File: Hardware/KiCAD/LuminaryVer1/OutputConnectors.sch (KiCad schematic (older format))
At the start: 2 parts, among them J13 CN1, J14 CN2

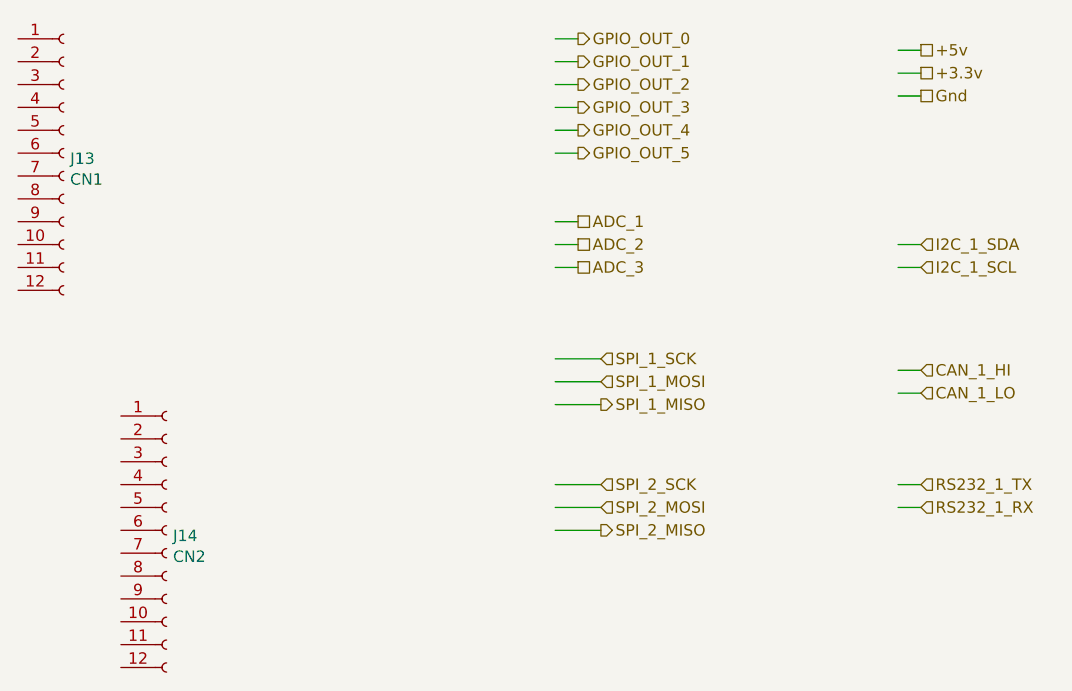
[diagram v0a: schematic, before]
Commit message: Added majority of the logic level circuitry. Almost done routing connections.
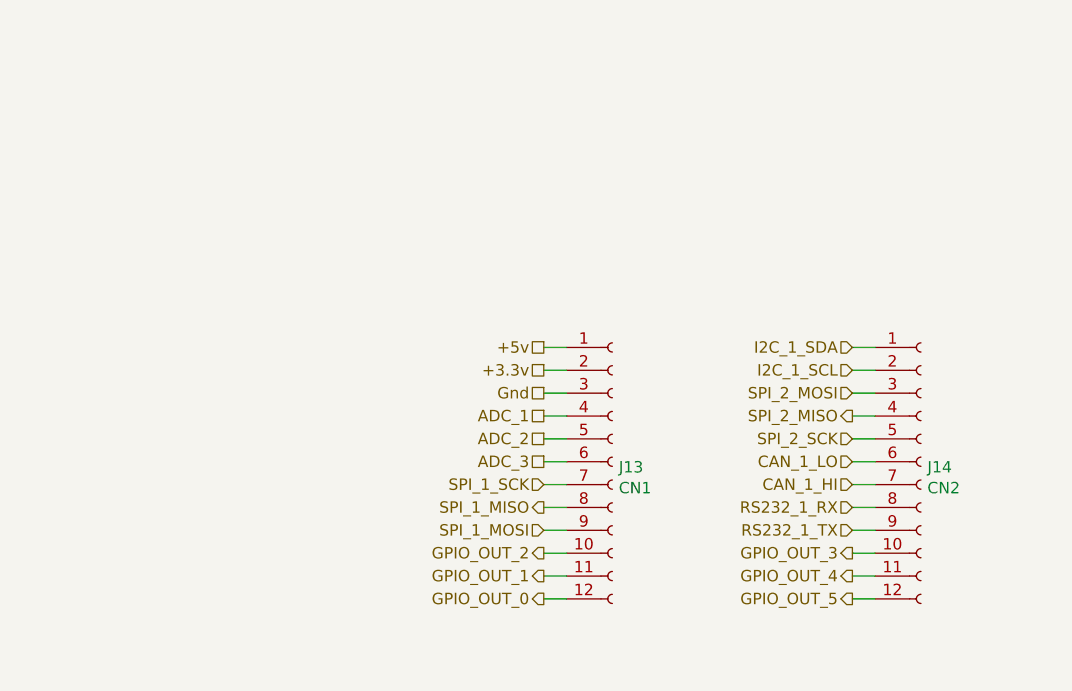
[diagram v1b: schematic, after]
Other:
- moved on the sheet: J13, J14
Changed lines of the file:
@@
 Comment4 ""
 $EndDescr
-Text HLabel 5100 3400 2    50   Input ~ 0
+Text HLabel 4850 3950 0    50   Input ~ 0
 SPI_1_SCK
-Text HLabel 5100 3500 2    50   Input ~ 0
+Text HLabel 4850 4150 0    50   Input ~ 0
 SPI_1_MOSI
-Text HLabel 5100 3600 2    50   Output ~ 0
+Text HLabel 4850 4050 0    50   Output ~ 0
 SPI_1_MISO
-Text HLabel 5100 3950 2    50   Input ~ 0
+Text HLabel 6200 3750 0    50   Input ~ 0
 SPI_2_SCK
-Text HLabel 5100 4050 2    50   Input ~ 0
+Text HLabel 6200 3550 0    50   Input ~ 0
 SPI_2_MOSI
-Text HLabel 5100 4150 2    50   Output ~ 0
+Text HLabel 6200 3650 0    50   Output ~ 0
 SPI_2_MISO
-Text HLabel 6500 2900 2    50   Input ~ 0
+Text HLabel 6200 3350 0    50   Input ~ 0
 I2C_1_SDA
-Text HLabel 6500 3000 2    50   Input ~ 0
+Text HLabel 6200 3450 0    50   Input ~ 0
 I2C_1_SCL
-Text HLabel 6500 3950 2    50   Input ~ 0
+Text HLabel 6200 4150 0    50   Input ~ 0
 RS232_1_TX
-Text HLabel 6500 4050 2    50   Input ~ 0
+Text HLabel 6200 4050 0    50   Input ~ 0
 RS232_1_RX
-Text HLabel 6500 3450 2    50   Input ~ 0
+Text HLabel 6200 3950 0    50   Input ~ 0
 CAN_1_HI
-Text HLabel 6500 3550 2    50   Input ~ 0
+Text HLabel 6200 3850 0    50   Input ~ 0
 CAN_1_LO
-Text HLabel 5000 2800 2    50   UnSpc ~ 0
+Text HLabel 4850 3650 0    50   UnSpc ~ 0
 ADC_1
-Text HLabel 5000 2900 2    50   UnSpc ~ 0
+Text HLabel 4850 3750 0    50   UnSpc ~ 0
 ADC_2
-Text HLabel 5000 3000 2    50   UnSpc ~ 0
+Text HLabel 4850 3850 0    50   UnSpc ~ 0
 ADC_3
-Wire Wire Line
-	4900 3400 5100 3400
-Wire Wire Line
-	4900 3500 5100 3500
-Wire Wire Line
-	4900 3600 5100 3600
-Wire Wire Line
-	4900 3950 5100 3950
-Wire Wire Line
-	4900 4050 5100 4050
-Wire Wire Line
-	4900 4150 5100 4150
-Wire Wire Line
-	6400 3450 6500 3450
-Wire Wire Line
-	6400 3550 6500 3550
-Wire Wire Line
-	4900 2800 5000 2800
-Wire Wire Line
-	4900 2900 5000 2900
-Wire Wire Line
-	4900 3000 5000 3000
-Wire Wire Line
-	6400 2900 6500 2900
-Wire Wire Line
-	6400 3000 6500 3000
-Wire Wire Line
-	6400 3950 6500 3950
-Wire Wire Line
-	6400 4050 6500 4050
-Text HLabel 5000 2000 2    50   Output ~ 0
+Text HLabel 4850 4450 0    50   Output ~ 0
 GPIO_OUT_0
-Text HLabel 5000 2100 2    50   Output ~ 0
+Text HLabel 4850 4350 0    50   Output ~ 0
 GPIO_OUT_1
-Text HLabel 5000 2200 2    50   Output ~ 0
+Text HLabel 4850 4250 0    50   Output ~ 0
 GPIO_OUT_2
-Text HLabel 5000 2300 2    50   Output ~ 0
+Text HLabel 6200 4250 0    50   Output ~ 0
 GPIO_OUT_3
-Text HLabel 5000 2400 2    50   Output ~ 0
+Text HLabel 6200 4350 0    50   Output ~ 0
 GPIO_OUT_4
-Text HLabel 5000 2500 2    50   Output ~ 0
+Text HLabel 6200 4450 0    50   Output ~ 0
 GPIO_OUT_5
-Wire Wire Line
-	4900 2000 5000 2000
-Wire Wire Line
-	4900 2100 5000 2100
-Wire Wire Line
-	4900 2200 5000 2200
-Wire Wire Line
-	4900 2300 5000 2300
-Wire Wire Line
-	4900 2400 5000 2400
-Wire Wire Line
-	4900 2500 5000 2500
-Text HLabel 6500 2050 2    50   UnSpc ~ 0
+Text HLabel 4850 3350 0    50   UnSpc ~ 0
 +5v
-Text HLabel 6500 2150 2    50   UnSpc ~ 0
+Text HLabel 4850 3450 0    50   UnSpc ~ 0
 +3.3v
-Text HLabel 6500 2250 2    50   UnSpc ~ 0
+Text HLabel 4850 3550 0    50   UnSpc ~ 0
 Gnd
-Wire Wire Line
-	6400 2250 6500 2250
-Wire Wire Line
-	6400 2150 6500 2150
-Wire Wire Line
-	6400 2050 6500 2050
 $Comp
 L Connector:Conn_01x12_Female J13
 U 1 1 5ECB3CF3
-P 2750 2500
-F 0 "J13" H 2778 2476 50  0000 L CNN
-F 1 "CN1" H 2778 2385 50  0000 L CNN
-F 2 "Connector_PinHeader_2.54mm:PinHeader_1x12_P2.54mm_Vertical" H 2750 2500 50  0001 C CNN
-F 3 "~" H 2750 2500 50  0001 C CNN
-	1    2750 2500
+P 5150 3850
+F 0 "J13" H 5178 3826 50  0000 L CNN
+F 1 "CN1" H 5178 3735 50  0000 L CNN
+F 2 "Connector_PinHeader_2.54mm:PinHeader_1x12_P2.54mm_Vertical" H 5150 3850 50  0001 C CNN
+F 3 "~" H 5150 3850 50  0001 C CNN
+	1    5150 3850
 	1    0    0    -1
 $EndComp
@@
 L Connector:Conn_01x12_Female J14
 U 1 1 5ECB51B2
-P 3200 4150
-F 0 "J14" H 3228 4126 50  0000 L CNN
-F 1 "CN2" H 3228 4035 50  0000 L CNN
-F 2 "Connector_PinHeader_2.54mm:PinHeader_1x12_P2.54mm_Vertical" H 3200 4150 50  0001 C CNN
-F 3 "~" H 3200 4150 50  0001 C CNN
-	1    3200 4150
+P 6500 3850
+F 0 "J14" H 6528 3826 50  0000 L CNN
+F 1 "CN2" H 6528 3735 50  0000 L CNN
+F 2 "Connector_PinHeader_2.54mm:PinHeader_1x12_P2.54mm_Vertical" H 6500 3850 50  0001 C CNN
+F 3 "~" H 6500 3850 50  0001 C CNN
+	1    6500 3850
 	1    0    0    -1
 $EndComp
+Wire Wire Line
+	6200 4250 6300 4250
+Wire Wire Line
+	6200 4350 6300 4350
+Wire Wire Line
+	6200 4450 6300 4450
+Wire Wire Line
+	4850 4250 4950 4250
+Wire Wire Line
+	4850 4350 4950 4350
+Wire Wire Line
+	4850 4450 4950 4450
+Wire Wire Line
+	4850 3350 4950 3350
+Wire Wire Line
+	4850 3450 4950 3450
+Wire Wire Line
+	4850 3550 4950 3550
+Wire Wire Line
+	4850 3650 4950 3650
+Wire Wire Line
+	4850 3750 4950 3750
+Wire Wire Line
+	4850 3850 4950 3850
+Wire Wire Line
+	4850 3950 4950 3950
+Wire Wire Line
+	4850 4050 4950 4050
+Wire Wire Line
+	4850 4150 4950 4150
+Wire Wire Line
+	6300 4050 6200 4050
+Wire Wire Line
+	6200 4150 6300 4150
+Wire Wire Line
+	6200 3950 6300 3950
+Wire Wire Line
+	6200 3850 6300 3850
+Wire Wire Line
+	6200 3350 6300 3350
+Wire Wire Line
+	6200 3450 6300 3450
+Wire Wire Line
+	6200 3550 6300 3550
+Wire Wire Line
+	6200 3650 6300 3650
+Wire Wire Line
+	6200 3750 6300 3750
 $EndSCHEMATC
